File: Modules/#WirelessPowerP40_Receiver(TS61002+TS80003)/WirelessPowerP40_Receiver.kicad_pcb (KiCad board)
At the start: 4 copper layers, 53 x 53 mm, 162 parts, among them J1 Conn_01x02_Male, J2 I2C, J3 I2C, J4 I2C, J5 COIL 24uH, J6 Conn_01x02_Male, J7 Conn_01x02_Male, Q1 2N7002, Q2 2N7002, Q3 2N7002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

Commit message: fix routing
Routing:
- net +3V3: track 79.8 -> 80.4 mm
- net VAC1: vias 18 -> 16

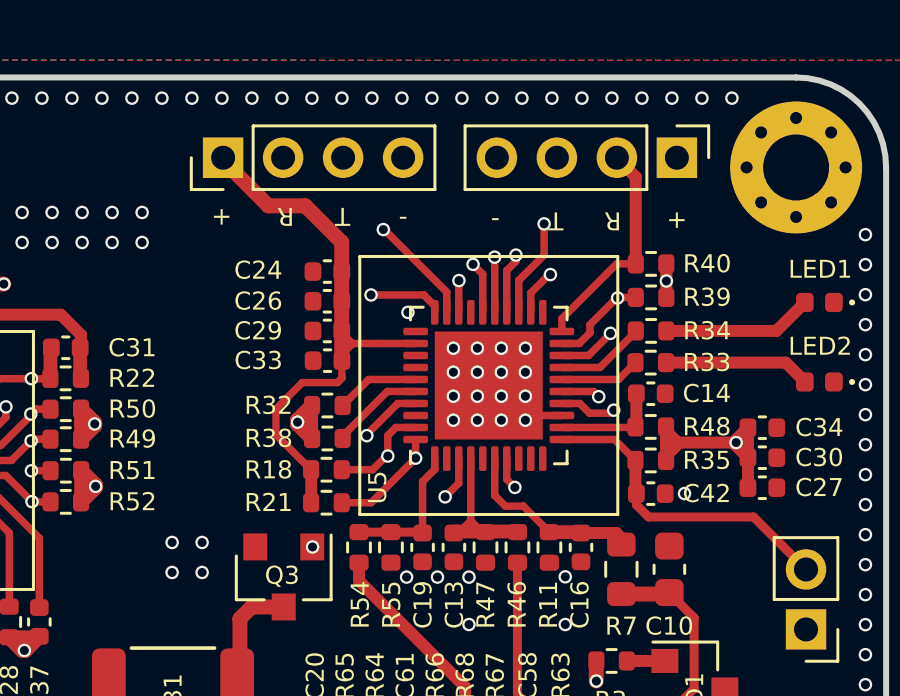
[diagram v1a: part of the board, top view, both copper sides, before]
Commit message: IO silk label fix
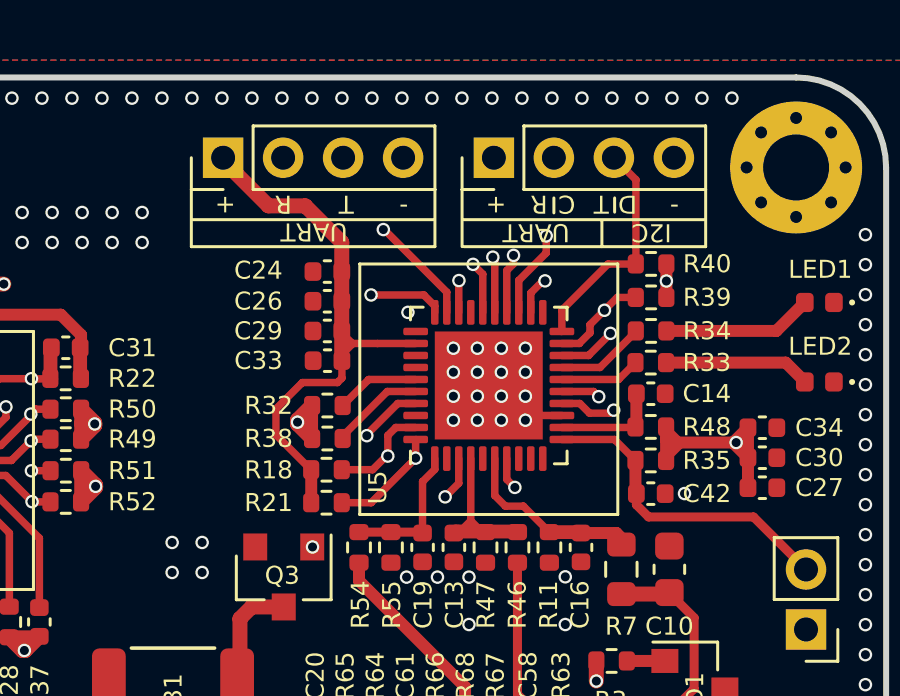
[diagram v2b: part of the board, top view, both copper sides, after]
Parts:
- C32: value 1nF -> 1nF 50V
- C58: value 22nF -> 22nF 50V
- D3: value BAS21-03W -> BAS21
- moved J2 6.10 mm to (148.7, 71.2), turned to 90 degrees
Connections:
- J2 pad 2: Net-(J2-Pad2) -> Net-(R39-Pad2)
- R39 pad 2: Net-(J2-Pad3) -> Net-(R39-Pad2)
- R40 pad 2: Net-(J2-Pad2) -> Net-(J2-Pad3)
- U5 pad 19: Net-(J2-Pad3) -> Net-(R39-Pad2)
- U5 pad 20: Net-(J2-Pad2) -> Net-(J2-Pad3)
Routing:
- net Net-(R39-Pad2): track 0.00 -> 9.04 mm, vias 0 -> 1
- net Net-(J2-Pad2): track 7.45 -> 0.00 mm
- net Net-(J2-Pad3): track 8.77 -> 7.66 mm, vias 1 -> 0
- net +3V3: track 80.4 -> 79.7 mm
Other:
- board text added: "C"
- board text added: "D"
- board text added: "I2C"
- board text added: "UART"

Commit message: re-saved by kicad6
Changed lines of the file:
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@@
   (net 64 "Net-(R25-Pad1)")
   (net 65 "Net-(D3-Pad3)")
-  (net 66 "Net-(R39-Pad2)")
+  (net 66 "Net-(J2-Pad2)")
   (net 67 "Net-(J2-Pad3)")
   (net 68 "Net-(J3-Pad2)")
@@
       (net 14 "+3V3") (pintype "passive"))
     (pad "2" smd roundrect locked (at 0.51 0 180) (size 0.54 0.64) (layers "F.Cu" "F.Paste" "F.Mask") (roundrect_rratio 0.25)
-      (net 66 "Net-(R39-Pad2)") (pintype "passive"))
+      (net 66 "Net-(J2-Pad2)") (pintype "passive"))
     (model "${KISYS3DMOD}/Resistor_SMD.3dshapes/R_0402_1005Metric.wrl"
       (offset (xyz 0 0 0))
@@
       (net 14 "+3V3") (pinfunction "Pin_1") (pintype "passive"))
     (pad "2" thru_hole oval locked (at 0 2 90) (size 1.35 1.35) (drill 0.8) (layers *.Cu *.Mask)
-      (net 66 "Net-(R39-Pad2)") (pinfunction "Pin_2") (pintype "passive"))
+      (net 66 "Net-(J2-Pad2)") (pinfunction "Pin_2") (pintype "passive"))
     (pad "3" thru_hole oval locked (at 0 4 90) (size 1.35 1.35) (drill 0.8) (layers *.Cu *.Mask)
       (net 67 "Net-(J2-Pad3)") (pinfunction "Pin_3") (pintype "passive"))
@@
       (net 102 "EN_DRV") (pinfunction "DRV_EN") (pintype "output"))
     (pad "19" smd roundrect locked (at 1.4 2.4375 90) (size 0.25 0.825) (layers "F.Cu" "F.Paste" "F.Mask") (roundrect_rratio 0.25)
-      (net 66 "Net-(R39-Pad2)") (pinfunction "I2C|SCL") (pintype "input"))
+      (net 66 "Net-(J2-Pad2)") (pinfunction "I2C|SCL") (pintype "input"))
     (pad "20" smd roundrect locked (at 1.8 2.4375 90) (size 0.25 0.825) (layers "F.Cu" "F.Paste" "F.Mask") (roundrect_rratio 0.25)
       (net 67 "Net-(J2-Pad3)") (pinfunction "I2C|SDA") (pintype "input"))
@@
   (segment (start 152.838214 75.831786) (end 153.455 75.831786) (width 0.25) (layer "F.Cu") (net 66))
   (via (at 152.41 76.26) (size 0.45) (drill 0.3) (layers "F.Cu" "B.Cu") (net 66))
-  (segment (start 152.41 76.26) (end 152.41 72.86) (width 0.25) (layer "In1.Cu") (net 66))
-  (segment (start 152.41 72.86) (end 150.725 71.175) (width 0.25) (layer "In1.Cu") (net 66))
+  (segment (start 152.41 76.26) (end 152.41 72.86) (width 0.3) (layer "In1.Cu") (net 66))
+  (segment (start 152.41 72.86) (end 150.725 71.175) (width 0.3) (layer "In1.Cu") (net 66))
   (segment (start 150.9925 76.967501) (end 150.9925 76.2575) (width 0.25) (layer "F.Cu") (net 67))
-  (segment (start 153.46 71.91) (end 153.46 74.71) (width 0.25) (layer "F.Cu") (net 67))
-  (segment (start 152.53 74.72) (end 153.47 74.72) (width 0.25) (layer "F.Cu") (net 67))
-  (segment (start 152.725 71.175) (end 153.46 71.91) (width 0.25) (layer "F.Cu") (net 67))
+  (segment (start 153.46 71.91) (end 153.46 74.71) (width 0.3) (layer "F.Cu") (net 67))
+  (segment (start 152.53 74.72) (end 153.47 74.72) (width 0.3) (layer "F.Cu") (net 67))
+  (segment (start 152.725 71.175) (end 153.46 71.91) (width 0.3) (layer "F.Cu") (net 67))
   (segment (start 150.9925 76.2575) (end 152.53 74.72) (width 0.25) (layer "F.Cu") (net 67))
   (segment (start 145.19 81.12) (end 145.14 81.12) (width 0.25) (layer "F.Cu") (net 68))
@@
   (segment (start 147.28 70.64) (end 146.57 69.93) (width 0.3) (layer "In2.Cu") (net 79))
   (segment (start 146.57 69.93) (end 131.84 69.93) (width 0.3) (layer "In2.Cu") (net 79))
-  (segment (start 131.84 69.93) (end 112.67 89.1) (width 0.3) (layer "In2.Cu") (net 79))
-  (segment (start 112.67 89.1) (end 112.67 105.42) (width 0.3) (layer "In2.Cu") (net 79))
+  (segment (start 131.84 69.93) (end 112.67 89.1) (width 0.5) (layer "In2.Cu") (net 79))
+  (segment (start 112.67 89.1) (end 112.67 105.42) (width 0.5) (layer "In2.Cu") (net 79))
   (segment (start 144.49 80.44) (end 144.49 80.4) (width 0.25) (layer "F.Cu") (net 80))
   (segment (start 145.522499 79.367501) (end 146.1175 79.367501) (width 0.25) (layer "F.Cu") (net 80))

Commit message: fix fatal error
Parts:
- added D4: 1N5819WT, Diode_SMD:D_SOD-523, F.Cu at (128.0, 75.7)
- moved R17 1.98 mm to (126.7, 75.9), turned to -90 degrees
- moved L2 1.23 mm to (124.4, 75.1), turned to 0 degrees
- moved C35 0.82 mm to (129.2, 75.9), turned to 90 degrees
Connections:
- C25 pad 2: VDDA -> GND
- C28 pad 2: VDDA -> GND
- C35 pad 1: +3V3 -> Net-(C35-Pad1)
- C35 pad 2: VDDA -> GND
- U4 pad 13: VDDA -> GND
- U4 pad 17: +3V3 -> Net-(C35-Pad1)
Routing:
- net VDDA: track 74.4 -> 58.3 mm, vias 5 -> 3
- net Net-(C35-Pad1): track 0.00 -> 3.79 mm
- net EN_GAIN: track 29.3 -> 26.7 mm
- net EN_DRV: track 43.4 -> 40.9 mm
- net +3V3: track 79.7 -> 77.6 mm
- net GND: track 7.31 -> 9.25 mm, vias 280 -> 281
- net EN_MOD: track 71.0 -> 71.6 mm

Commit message: sch prettify
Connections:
- net VCC renamed Net-(C1-Pad1)
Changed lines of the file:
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@@
   (net 5 "Net-(C11-Pad1)")
   (net 6 "Net-(C11-Pad2)")
-  (net 7 "VCC")
+  (net 7 "Net-(C1-Pad1)")
   (net 8 "Net-(LED3-Pad2)")
   (net 9 "+5V")
@@
     (pad "" smd roundrect locked (at 0.425 -0.425) (size 0.69 0.69) (layers "F.Paste") (roundrect_rratio 0.25))
     (pad "1" smd roundrect locked (at -1.4625 -0.75) (size 0.825 0.25) (layers "F.Cu" "F.Paste" "F.Mask") (roundrect_rratio 0.25)
-      (net 6 "Net-(C11-Pad2)") (pinfunction "VSW") (pintype "output"))
+      (net 6 "Net-(C11-Pad2)") (pinfunction "VSW") (pintype "passive"))
     (pad "2" smd roundrect locked (at -1.4625 -0.25) (size 0.825 0.25) (layers "F.Cu" "F.Paste" "F.Mask") (roundrect_rratio 0.25)
-      (net 7 "VCC") (pinfunction "VCC") (pintype "power_in"))
+      (net 7 "Net-(C1-Pad1)") (pinfunction "VCC") (pintype "passive"))
     (pad "3" smd roundrect locked (at -1.4625 0.25) (size 0.825 0.25) (layers "F.Cu" "F.Paste" "F.Mask") (roundrect_rratio 0.25)
-      (net 7 "VCC") (pinfunction "VCC") (pintype "power_in"))
+      (net 7 "Net-(C1-Pad1)") (pinfunction "VCC") (pintype "passive"))
     (pad "4" smd roundrect locked (at -1.4625 0.75) (size 0.825 0.25) (layers "F.Cu" "F.Paste" "F.Mask") (roundrect_rratio 0.25)
-      (net 1 "GND") (pinfunction "GND") (pintype "input"))
+      (net 1 "GND") (pinfunction "GND") (pintype "passive"))
     (pad "5" smd roundrect locked (at -0.75 1.4625) (size 0.25 0.825) (layers "F.Cu" "F.Paste" "F.Mask") (roundrect_rratio 0.25)
       (net 28 "Net-(R13-Pad1)") (pinfunction "FB") (pintype "input"))
@@
       (net 5 "Net-(C11-Pad1)") (pinfunction "BST") (pintype "output"))
     (pad "11" smd roundrect locked (at 1.4625 -0.25) (size 0.825 0.25) (layers "F.Cu" "F.Paste" "F.Mask") (roundrect_rratio 0.25)
-      (net 7 "VCC") (pinfunction "VCC") (pintype "power_in"))
+      (net 7 "Net-(C1-Pad1)") (pinfunction "VCC") (pintype "passive"))
     (pad "12" smd roundrect locked (at 1.4625 -0.75) (size 0.825 0.25) (layers "F.Cu" "F.Paste" "F.Mask") (roundrect_rratio 0.25)
-      (net 6 "Net-(C11-Pad2)") (pinfunction "VSW") (pintype "output"))
+      (net 6 "Net-(C11-Pad2)") (pinfunction "VSW") (pintype "passive"))
     (pad "13" smd roundrect locked (at 0.75 -1.4625) (size 0.25 0.825) (layers "F.Cu" "F.Paste" "F.Mask") (roundrect_rratio 0.25)
-      (net 6 "Net-(C11-Pad2)") (pinfunction "VSW") (pintype "output"))
+      (net 6 "Net-(C11-Pad2)") (pinfunction "VSW") (pintype "passive"))
     (pad "14" smd roundrect locked (at 0.25 -1.4625) (size 0.25 0.825) (layers "F.Cu" "F.Paste" "F.Mask") (roundrect_rratio 0.25)
-      (net 1 "GND") (pinfunction "GND") (pintype "input"))
+      (net 1 "GND") (pinfunction "GND") (pintype "passive"))
     (pad "15" smd roundrect locked (at -0.25 -1.4625) (size 0.25 0.825) (layers "F.Cu" "F.Paste" "F.Mask") (roundrect_rratio 0.25)
-      (net 1 "GND") (pinfunction "GND") (pintype "input"))
+      (net 1 "GND") (pinfunction "GND") (pintype "passive"))
     (pad "16" smd roundrect locked (at -0.75 -1.4625) (size 0.25 0.825) (layers "F.Cu" "F.Paste" "F.Mask") (roundrect_rratio 0.25)
-      (net 6 "Net-(C11-Pad2)") (pinfunction "VSW") (pintype "output"))
+      (net 6 "Net-(C11-Pad2)") (pinfunction "VSW") (pintype "passive"))
     (pad "17" smd rect locked (at 0 0) (size 1.7 1.7) (layers "F.Cu" "F.Mask")
-      (net 1 "GND") (pinfunction "GND") (pintype "input"))
+      (net 1 "GND") (pinfunction "GND") (pintype "passive"))
     (model "${KICAD6_3DMODEL_DIR}/Package_DFN_QFN.3dshapes/QFN-16-1EP_3x3mm_P0.5mm_EP1.7x1.7mm.wrl"
       (offset (xyz 0 0 0))
@@
     (fp_line (start 0.5 -0.25) (end 0.5 0.25) (layer "F.Fab") (width 0.1))
     (pad "1" smd roundrect locked (at -0.48 0 90) (size 0.56 0.62) (layers "F.Cu" "F.Paste" "F.Mask") (roundrect_rratio 0.25)
-      (net 7 "VCC") (pintype "passive"))
+      (net 7 "Net-(C1-Pad1)") (pintype "passive"))
     (pad "2" smd roundrect locked (at 0.48 0 90) (size 0.56 0.62) (layers "F.Cu" "F.Paste" "F.Mask") (roundrect_rratio 0.25)
       (net 1 "GND") (pintype "passive"))
@@
       (net 97 "Net-(R64-Pad2)") (pinfunction "VOUT") (pintype "input"))
     (pad "3" smd roundrect locked (at -1.45 0 270) (size 0.85 0.2) (layers "F.Cu" "F.Paste" "F.Mask") (roundrect_rratio 0.25)
-      (net 9 "+5V") (pinfunction "VDDA") (pintype "output"))
+      (net 9 "+5V") (pinfunction "VDDA") (pintype "passive"))
     (pad "4" smd roundrect locked (at -1.45 0.4 270) (size 0.85 0.2) (layers "F.Cu" "F.Paste" "F.Mask") (roundrect_rratio 0.25)
       (net 10 "Net-(C20-Pad2)") (pinfunction "VLDO") (pintype "output"))
@@
       (net 65 "Net-(D3-Pad3)") (pinfunction "LX") (pintype "output"))
     (pad "11" smd roundrect locked (at 1.45 0.8 270) (size 0.85 0.2) (layers "F.Cu" "F.Paste" "F.Mask") (roundrect_rratio 0.25)
-      (net 1 "GND") (pinfunction "PGND") (pintype "output"))
+      (net 1 "GND") (pinfunction "PGND") (pintype "passive"))
     (pad "12" smd roundrect locked (at 1.45 0.4 270) (size 0.85 0.2) (layers "F.Cu" "F.Paste" "F.Mask") (roundrect_rratio 0.25)
       (net 96 "Net-(R58-Pad2)") (pinfunction "DL") (pintype "output"))
     (pad "13" smd roundrect locked (at 1.45 0 270) (size 0.85 0.2) (layers "F.Cu" "F.Paste" "F.Mask") (roundrect_rratio 0.25)
-      (net 9 "+5V") (pinfunction "VDDP") (pintype "output"))
+      (net 9 "+5V") (pinfunction "VDDP") (pintype "passive"))
     (pad "14" smd roundrect locked (at 1.45 -0.4 270) (size 0.85 0.2) (layers "F.Cu" "F.Paste" "F.Mask") (roundrect_rratio 0.25)
       (net 9 "+5V") (pinfunction "PSV") (pintype "output"))
@@
       (net 95 "Net-(R57-Pad2)") (pinfunction "LIMI") (pintype "output"))
     (pad "17" smd roundrect locked (at 0.4 -1.45 270) (size 0.2 0.85) (layers "F.Cu" "F.Paste" "F.Mask") (roundrect_rratio 0.25)
-      (net 99 "EN_LOAD") (pinfunction "EN") (pintype "output"))
+      (net 99 "EN_LOAD") (pinfunction "EN") (pintype "input"))
     (pad "18" smd roundrect locked (at 0 -1.45 270) (size 0.2 0.85) (layers "F.Cu" "F.Paste" "F.Mask") (roundrect_rratio 0.25)
-      (net 1 "GND") (pinfunction "AGND") (pintype "output"))
+      (net 1 "GND") (pinfunction "AGND") (pintype "passive"))
     (pad "19" smd roundrect locked (at -0.4 -1.45 270) (size 0.2 0.85) (layers "F.Cu" "F.Paste" "F.Mask") (roundrect_rratio 0.25)
       (net 93 "Net-(R53-Pad2)") (pinfunction "TON") (pintype "output"))
     (pad "20" smd roundrect locked (at -0.8 -1.45 270) (size 0.2 0.85) (layers "F.Cu" "F.Paste" "F.Mask") (roundrect_rratio 0.25)
-      (net 1 "GND") (pinfunction "ENL") (pintype "output"))
+      (net 1 "GND") (pinfunction "ENL") (pintype "input"))
     (pad "21" smd rect locked (at 0 0 270) (size 1.65 1.65) (layers "F.Cu" "F.Mask")
-      (net 1 "GND") (pinfunction "EP") (pintype "output"))
+      (net 1 "GND") (pinfunction "EP") (pintype "passive"))
     (model "${KISYS3DMOD}/Package_DFN_QFN.3dshapes/QFN-20-1EP_3x3mm_P0.4mm_EP1.65x1.65mm.wrl"
       (offset (xyz 0 0 0))
@@
     (fp_line (start 0.525 0.27) (end -0.525 0.27) (layer "F.Fab") (width 0.1))
     (pad "1" smd roundrect locked (at -0.51 0 270) (size 0.54 0.64) (layers "F.Cu" "F.Paste" "F.Mask") (roundrect_rratio 0.25)
-      (net 7 "VCC") (pintype "passive"))
+      (net 7 "Net-(C1-Pad1)") (pintype "passive"))
     (pad "2" smd roundrect locked (at 0.51 0 270) (size 0.54 0.64) (layers "F.Cu" "F.Paste" "F.Mask") (roundrect_rratio 0.25)
       (net 84 "Net-(R4-Pad2)") (pintype "passive"))
@@
       (net 78 "Net-(Q1-Pad1)") (pinfunction "G") (pintype "input"))
     (pad "2" smd rect locked (at -1 0.95 180) (size 0.9 0.8) (layers "F.Cu" "F.Paste" "F.Mask")
-      (net 7 "VCC") (pinfunction "S") (pintype "passive"))
+      (net 7 "Net-(C1-Pad1)") (pinfunction "S") (pintype "passive"))
     (pad "3" smd rect locked (at 1 0 180) (size 0.9 0.8) (layers "F.Cu" "F.Paste" "F.Mask")
       (net 11 "HT") (pinfunction "D") (pintype "passive"))
